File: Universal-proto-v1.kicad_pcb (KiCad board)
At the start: 2 copper layers, 81.5 x 121 mm, 45 parts, among them J1 Bus_ISA_8bit, J2 ISA Breakout, J3 Pico GPIO Breakout 2, J4 Pico GPIO Breakout 1

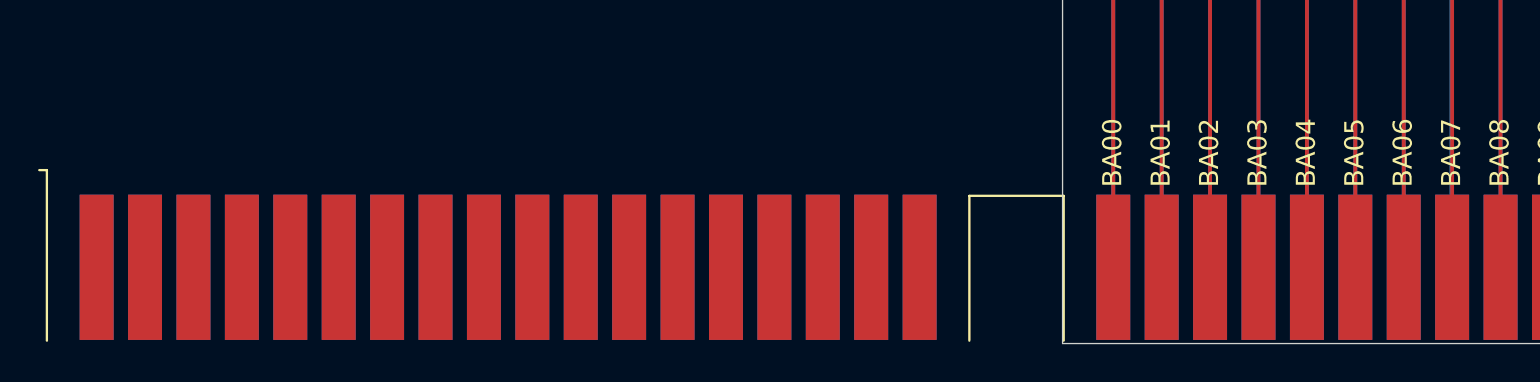
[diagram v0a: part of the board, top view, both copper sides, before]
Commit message: Created 8bit ISA footprint in parts.pretty
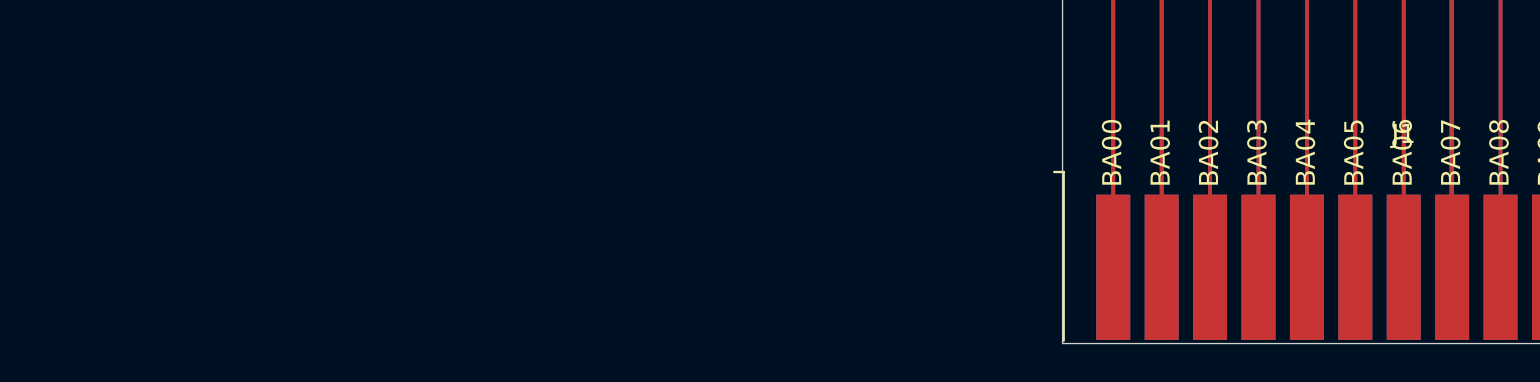
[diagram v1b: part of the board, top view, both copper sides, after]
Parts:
- J1: footprint Connector_PCBEdge:BUS_AT -> parts:ISA_8bit

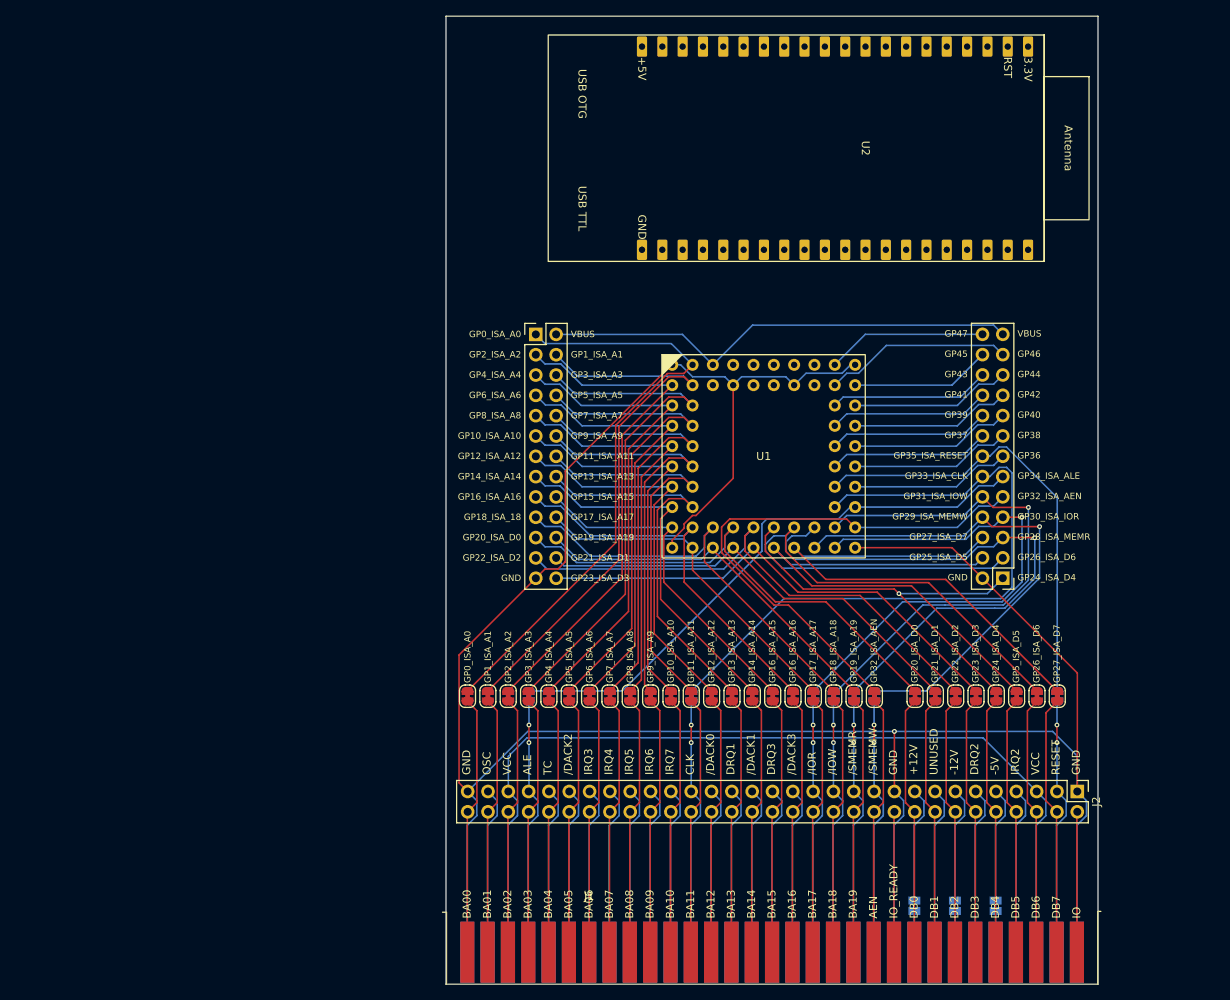
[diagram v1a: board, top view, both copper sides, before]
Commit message: Added logos
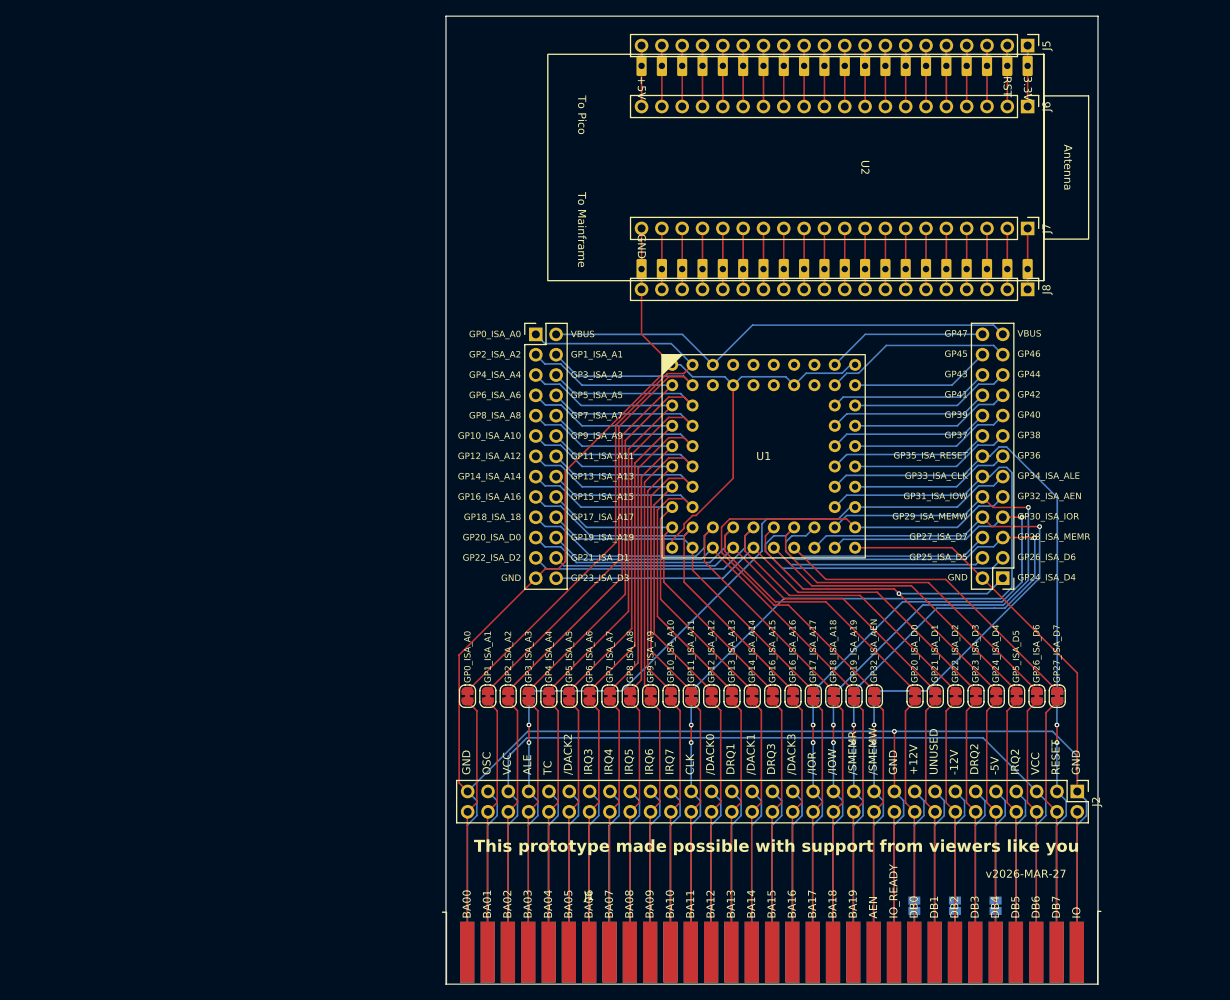
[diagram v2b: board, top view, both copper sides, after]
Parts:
- added J5: Conn_01x20, Connector_PinHeader_2.54mm:PinHeader_1x20_P2.54mm_Vertical, F.Cu at (179.7, 26.7)
- added J6: Conn_01x20, Connector_PinHeader_2.54mm:PinHeader_1x20_P2.54mm_Vertical, F.Cu at (179.7, 34.3)
- added J7: Conn_01x20, Connector_PinHeader_2.54mm:PinHeader_1x20_P2.54mm_Vertical, F.Cu at (179.7, 49.5)
- added J8: Conn_01x20, Connector_PinHeader_2.54mm:PinHeader_1x20_P2.54mm_Vertical, F.Cu at (179.7, 57.1)
- moved U2 2.41 mm to (179.7, 29.2)
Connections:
- U2 pad 3V3: unconnected-(U2-Pad3V3) -> /E_3v3
- U2 pad 5V: unconnected-(U2-Pad5V) -> /E_5V
- U2 pad EN: unconnected-(U2-RST-PadEN) -> /E_EN
- U2 pad G0: unconnected-(U2-GPIO0-PadG0) -> /E_GP0
- U2 pad G1: unconnected-(U2-GPIO1-PadG1) -> /E_GP1
- U2 pad G10: unconnected-(U2-GPIO10-PadG10) -> /E_GP10
- U2 pad G11: unconnected-(U2-GPIO11-PadG11) -> /E_GP11
- U2 pad G12: unconnected-(U2-GPIO12-PadG12) -> /E_GP12
- U2 pad G13: unconnected-(U2-GPIO13-PadG13) -> /E_GP13
- U2 pad G14: unconnected-(U2-GPIO14-PadG14) -> /E_GP14
- U2 pad G15: unconnected-(U2-GPIO15-PadG15) -> /E_GP15
- U2 pad G16: unconnected-(U2-GPIO16-PadG16) -> /E_GP16
- U2 pad G17: unconnected-(U2-GPIO17-PadG17) -> /E_GP17
- U2 pad G18: unconnected-(U2-GPIO18-PadG18) -> /E_GP18
- U2 pad G19: unconnected-(U2-GPIO19-PadG19) -> /E_GP19
- U2 pad G2: unconnected-(U2-GPIO2-PadG2) -> /E_GP2
- U2 pad G20: unconnected-(U2-GPIO20-PadG20) -> /E_GP20
- U2 pad G21: unconnected-(U2-GPIO21-PadG21) -> /E_GP21
- U2 pad G3: unconnected-(U2-GPIO3-PadG3) -> /E_GP3
- U2 pad G35: unconnected-(U2-GPIO35-PadG35) -> /E_GP35
- U2 pad G36: unconnected-(U2-GPIO36-PadG36) -> /E_GP36
- U2 pad G37: unconnected-(U2-GPIO37-PadG37) -> /E_GP37
- U2 pad G38: unconnected-(U2-GPIO38-PadG38) -> /E_GP38
- U2 pad G39: unconnected-(U2-GPIO39-PadG39) -> /E_GP39
- U2 pad G4: unconnected-(U2-GPIO4-PadG4) -> /E_GP4
- U2 pad G40: unconnected-(U2-GPIO40-PadG40) -> /E_GP40
- U2 pad G41: unconnected-(U2-GPIO41-PadG41) -> /E_GP41
- U2 pad G42: unconnected-(U2-GPIO42-PadG42) -> /E_GP42
- U2 pad G43: unconnected-(U2-GPIO43-PadG43) -> /E_TX
- U2 pad G44: unconnected-(U2-GPIO44-PadG44) -> /E_RX
- U2 pad G45: unconnected-(U2-GPIO45-PadG45) -> /E_GP45
- U2 pad G46: unconnected-(U2-GPIO46-PadG46) -> /E_GP46
- U2 pad G47: unconnected-(U2-GPIO47-PadG47) -> /E_GP47
- U2 pad G48: unconnected-(U2-GPIO48-PadG48) -> /E_GP48
- U2 pad G5: unconnected-(U2-GPIO5-PadG5) -> /E_GP5
- U2 pad G6: unconnected-(U2-GPIO6-PadG6) -> /E_GP6
- U2 pad G7: unconnected-(U2-GPIO7-PadG7) -> /E_GP7
- U2 pad G8: unconnected-(U2-GPIO8-PadG8) -> /E_GP8
- U2 pad G9: unconnected-(U2-GPIO9-PadG9) -> /E_GP9
- U2 pad GND: unconnected-(U2-PadGND) -> /GND
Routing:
- net /GND: track 320.2 -> 338.8 mm
- net /E_TX: track 0.00 -> 7.62 mm
- net /E_RX: track 0.00 -> 7.62 mm
- net /E_GP9: track 0.00 -> 7.62 mm
- net /E_GP8: track 0.00 -> 7.62 mm
- net /E_GP7: track 0.00 -> 7.62 mm
- net /E_GP6: track 0.00 -> 7.62 mm
- net /E_GP5: track 0.00 -> 7.62 mm
- net /E_GP48: track 0.00 -> 7.62 mm
- net /E_GP47: track 0.00 -> 7.62 mm
- net /E_GP46: track 0.00 -> 7.62 mm
- net /E_GP45: track 0.00 -> 7.62 mm
- net /E_GP42: track 0.00 -> 7.62 mm
- net /E_GP41: track 0.00 -> 7.62 mm
- net /E_GP40: track 0.00 -> 7.62 mm
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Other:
- board text added: "This prototype made possible with support from viewers like you"
- board text added: "v2026-MAR-27"

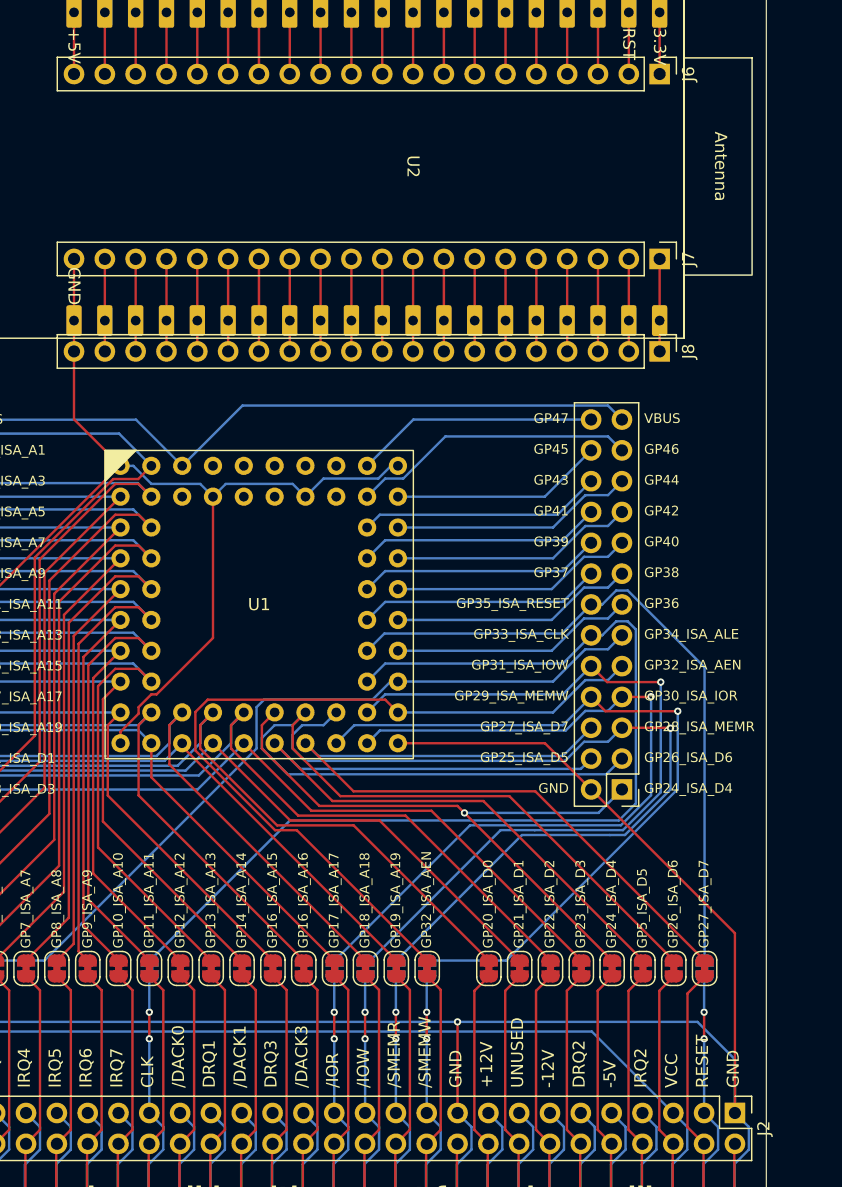
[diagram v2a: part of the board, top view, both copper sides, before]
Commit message: Added warning, diode, jumpers for 5V from edge
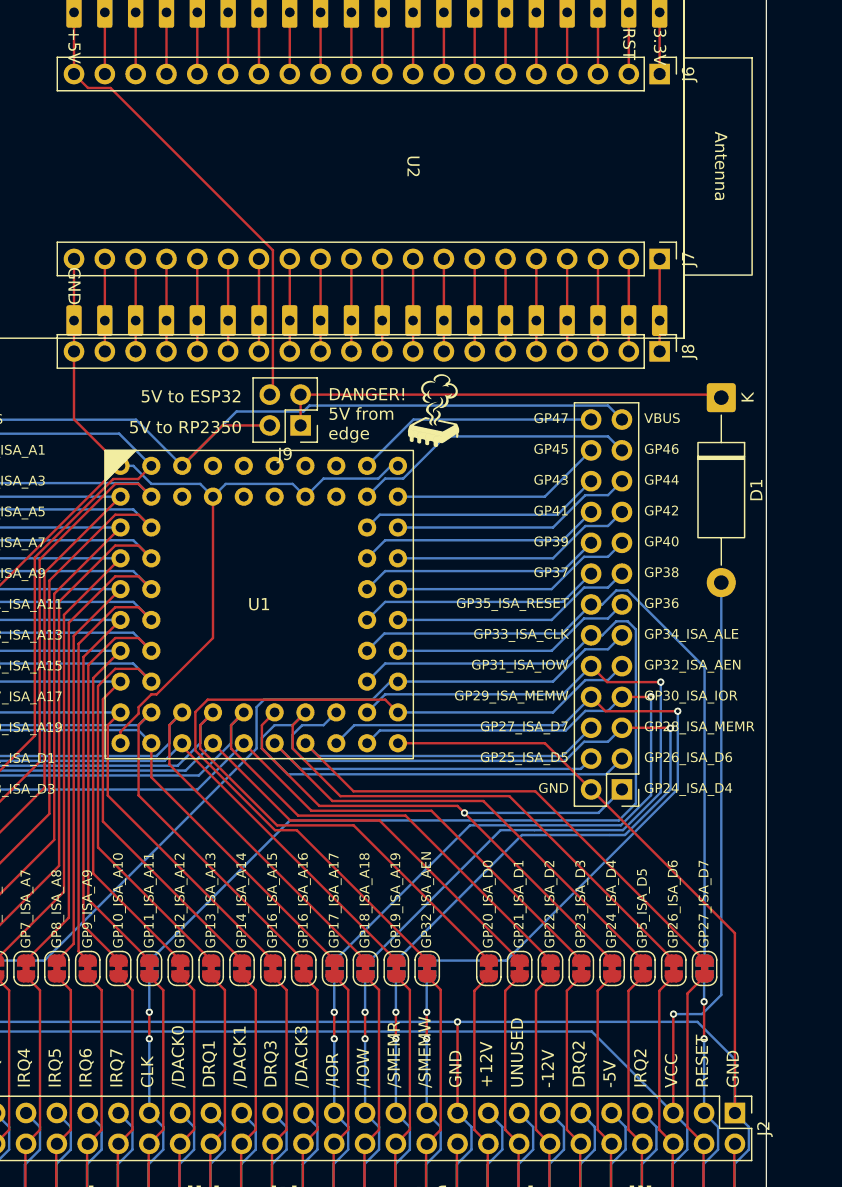
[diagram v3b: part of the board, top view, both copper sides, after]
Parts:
- added D1: D, Diode_THT:D_DO-15_P15.24mm_Horizontal, F.Cu at (184.8, 61.0)
- added J9: Conn_02x02_Odd_Even, Connector_PinHeader_2.54mm:PinHeader_2x02_P2.54mm_Vertical, F.Cu at (150.1, 63.3)
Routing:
- net /VCC: track 116.3 -> 163.0 mm, vias 0 -> 1
- net Net-(D1-K): track 0.00 -> 37.3 mm
- net /E_5V: track 7.62 -> 42.0 mm
- net /VBUS: track 59.9 -> 68.5 mm
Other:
- board text added: "5V to ESP32"
- board text added: "5V to RP2350"
- board text added: "DANGER! 5V from edge"

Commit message: Cleanups
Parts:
- moved J5 0.76 mm to (179.7, 25.9)
- moved J6 0.76 mm to (179.7, 33.5)
- moved J7 0.76 mm to (179.7, 48.8)
- moved J8 0.76 mm to (179.7, 56.4)
- moved U2 0.76 mm to (179.7, 28.4)
- moved J9 0.13 mm to (150.1, 63.1)
